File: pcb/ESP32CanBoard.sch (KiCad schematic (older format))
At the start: 46 parts, among them K1 1Wire, P1 Voltages, P101 CanBus, P2 Power, P3 CONN_1, P4 CONN_1, P5 CONN_1, P6 CONN_1, U1 ESP32Dev, U102 TJA1050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

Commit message: Just before switching away from ESP32 ADC
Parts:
- removed C5, C6: 100nF, Capacitors_SMD:C_0805_HandSoldering, symbol C
- removed JP1: ADC_CAL, Pin_Headers:Pin_Header_Straight_2x01, symbol JUMPER
- removed P1: Voltages, Connect:bornier6, symbol CONN_6
- removed R12, R13: 1M, Resistors_SMD:R_0805_HandSoldering, symbol R
- removed R5, R6: 220K, Resistors_SMD:R_0805_HandSoldering, symbol R
- added P102: CONN_4, Connect:bornier4, symbol CONN_4
- added U101: ADS1115, Divers:ADS1115, symbol ADS1115
- R1, R2, R3, R4: value 220K -> 22K
- R10, R7, R8, R9: value 1M -> 100K
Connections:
- net labels removed: ADC0, ADC1, ADC2, ADC3, ADC4, ADC5, DAC_Calibration, VIN0, VIN1, VIN2, VIN3, VIN4, VIN5
- wire segments 128 -> 106
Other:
- note added: "15*2.2/12.2=2.7049v\nRemove for shunt measurements"
- note added: "A0-A3 have ESD capable of sinking max 10mA. \nWith 100K that allows the inputs to see 1KV before any damage is done.\nHence no external diodes required.\nInternal resistance of the ADC at 4v FSD is 6M single ended, 15M double ended. At 0.256v Single ended the interal resistance is 100M\nBoth single and double ended will measure + - voltages."
- note added: "Measuring Voltage can be single ended, but measuring a shunt may\nhave to be differential since there will be voltage drop over the negative\nsupply line between the shunt and the pcd, unless the pcb has its -ve at the shunt."

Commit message: New board, moved bme280 to CanPressure board
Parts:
- removed C1, C2, C3, C4: 100nF, Capacitors_SMD:C_0805_HandSoldering, symbol C
- removed P101: CanBus, Connect:bornier2, symbol CONN_2
- removed P2: Power, Connect:bornier2, symbol CONN_2
- removed R1, R2, R3, R4: 22K, Resistors_SMD:R_0805_HandSoldering, symbol R
- removed R10, R7, R8, R9: 100K, Resistors_SMD:R_0805_HandSoldering, symbol R
- removed U101: ADS1115, Divers:ADS1115, symbol ADS1115
- removed U2: BMP280, Divers:BMP280, symbol BMP280
- added C101: 100nF, Capacitors_SMD:C_0805, symbol C
- added D103, D104: SMBJ30CA-TR TSV, Diodes_SMD:DO-214AB, symbol DIODE
- added D105: 1N5819, Diodes_SMD:D_1206, symbol DIODE
- added IC101: SP3481CN, Housings_SOIC:SOIC-8_3.9x4.9mm_Pitch1.27mm, symbol SP3481CN
- added P101: CAN, Connect:bornier4, symbol CONN_4
- added P103: Display, Pin_Headers:Pin_Header_Straight_1x05, symbol CONN_5
- added P104: Dsiplay, Pin_Headers:Pin_Header_Straight_1x08, symbol CONN_8
- added R101: 4K7, Resistors_SMD:R_0805, symbol R
- added TH101, TH102: Thermistor, Resistors_SMD:R_1812, symbol THERMISTOR
- C105: footprint Capacitors_SMD:C_0805_HandSoldering -> Capacitors_SMD:C_0805
- C205, C206: footprint Capacitors_SMD:C_1210_HandSoldering -> Capacitors_SMD:C_1210
- D101, D102, D203: footprint Diodes_SMD:DO-214AB_Handsoldering -> Diodes_SMD:DO-214AB
- D204: footprint Diodes_SMD:DO-214AB_Handsoldering -> Diodes_SMD:D_1206
- P102: value CONN_4 -> RS485
- R11, R14, R15, R16, R17: footprint Resistors_SMD:R_0805_HandSoldering -> Resistors_SMD:R_0805
- TH1, TH2: footprint Resistors_SMD:R_1210 -> Resistors_SMD:R_1812
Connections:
- net labels added: 5.8V, BL, BTN, CAN-H, CAN-L, CS, DC, MOSI, RS485-A, RS485-B, RS485-EN, RS485-RX, RS485-TX, RST, SCK
- wire segments 106 -> 113
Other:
- note removed: "15*2.2/12.2=2.7049v\nRemove for shunt measurements"
- note removed: "A0-A3 have ESD capable of sinking max 10mA. \nWith 100K that allows the inputs to see 1KV before any damage is done.\nHence no external diodes required.\nInternal resistance of the ADC at 4v FSD is 6M single ended, 15M double ended. At 0.256v Single ended the interal resistance is 100M\nBoth single and double ended will measure + - voltages."
- note removed: "Measuring Voltage can be single ended, but measuring a shunt may\nhave to be differential since there will be voltage drop over the negative\nsupply line between the shunt and the pcd, unless the pcb has its -ve at the shunt."

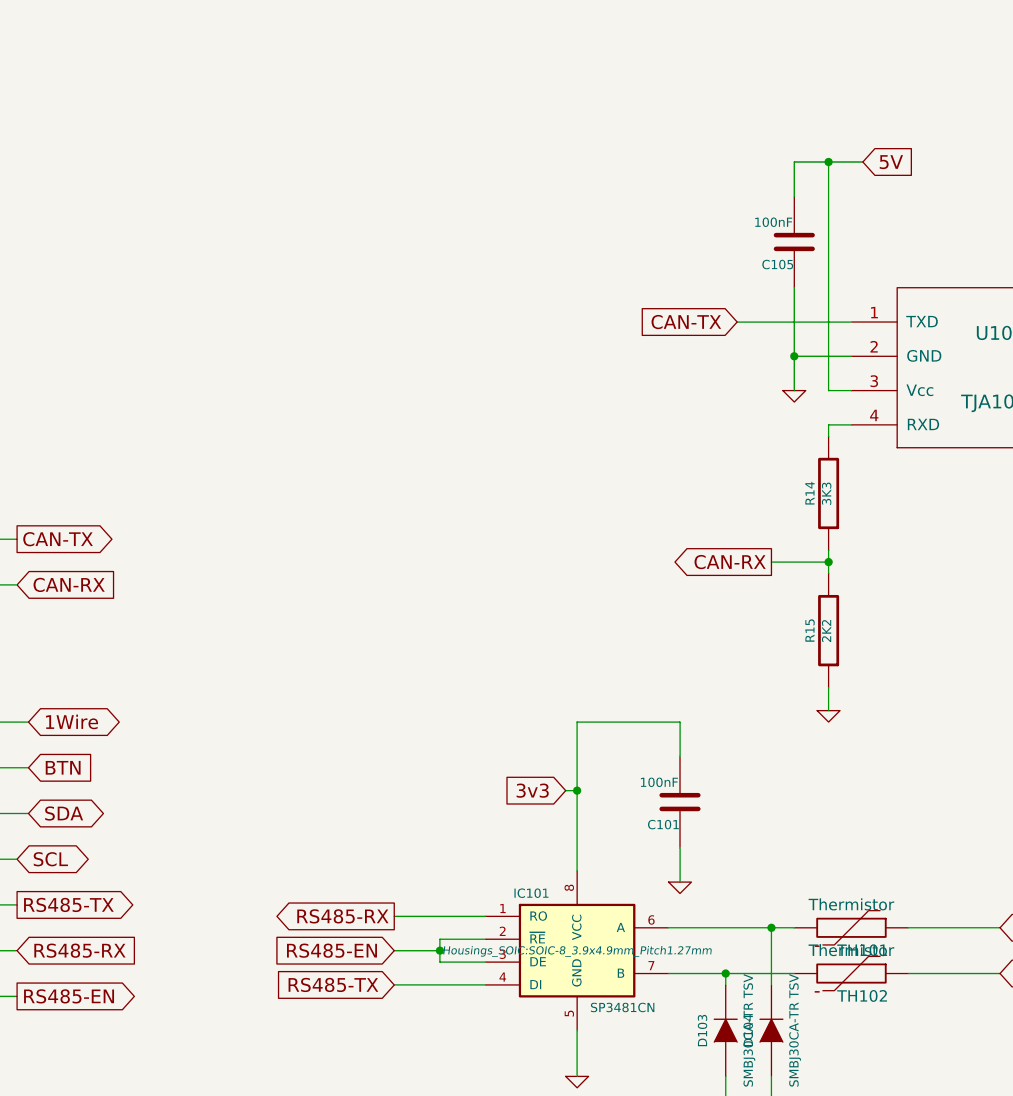
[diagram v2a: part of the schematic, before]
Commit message: New board operational using Modbus BatterySensors and CanPressure board
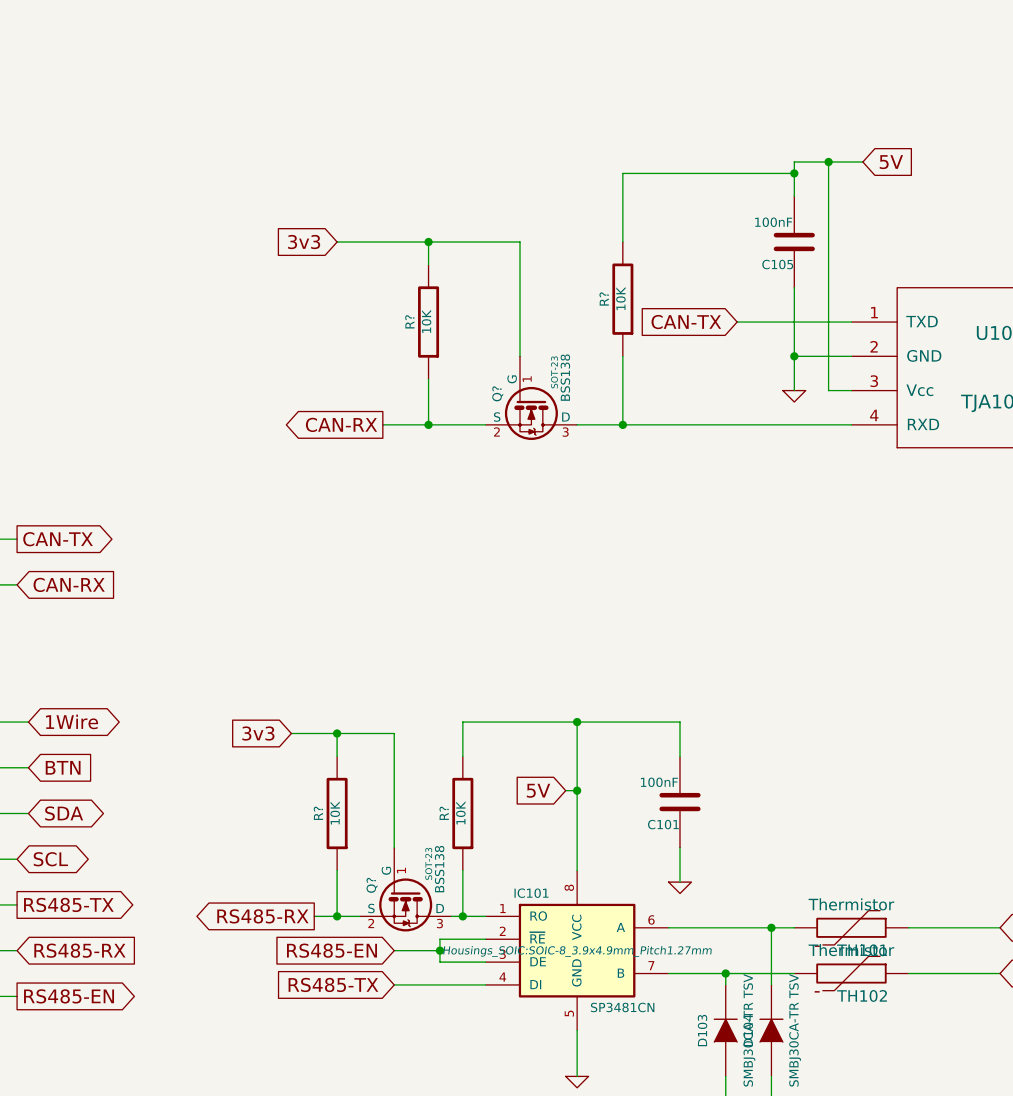
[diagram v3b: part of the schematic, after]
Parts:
- removed R14: 3K3, Resistors_SMD:R_0805, symbol R
- removed R15: 2K2, Resistors_SMD:R_0805, symbol R
- added Q? (x2): BSS138, SOT-23, symbol BSS138
- added R? (x4): 10K, Resistors_SMD:R_0805, symbol R
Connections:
- net 3v3: now also Q?.1 (G), Q?.1 (G), R?.2, R?.2; no longer C101.2, IC101.8 (VCC)
- net 5V: now also C101.2, IC101.8 (VCC), R?.2, R?.2
- net CAN-RX: now also Q?.2 (S), R?.1
- net RS485-RX: now also Q?.2 (S), R?.1; no longer IC101.1 (RO)
- net at U102.4 (RXD): now also Q?.3 (D), R?.1
- new net: IC101.1 (RO), Q?.3 (D), R?.1
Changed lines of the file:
@@
 Connection ~ 10650 3800
 Wire Wire Line
-	10650 3100 10650 2950
+	10650 2950 10650 3100
 Wire Wire Line
 	10650 2950 10950 2950
@@
 Text GLabel 10400 3650 0    60   Input ~ 0
 CAN-TX
-$Comp
-L R R14
-U 1 1 618128F6
-P 10800 4400
-F 0 "R14" V 10880 4400 40  0000 C CNN
-F 1 "3K3" V 10807 4401 40  0000 C CNN
-F 2 "Resistors_SMD:R_0805" V 10730 4400 30  0001 C CNN
-F 3 "" H 10800 4400 30  0000 C CNN
-	1    10800 4400
-	-1   0    0    1
-$EndComp
-$Comp
-L R R15
-U 1 1 618129BF
-P 10800 5000
-F 0 "R15" V 10880 5000 40  0000 C CNN
-F 1 "2K2" V 10807 5001 40  0000 C CNN
-F 2 "Resistors_SMD:R_0805" V 10730 5000 30  0001 C CNN
-F 3 "" H 10800 5000 30  0000 C CNN
-	1    10800 5000
-	-1   0    0    1
-$EndComp
-Wire Wire Line
-	10900 4100 10800 4100
-Wire Wire Line
-	10800 4100 10800 4150
-Wire Wire Line
-	10800 4650 10800 4750
-$Comp
-L GND #PWR010
-U 1 1 61812E4A
-P 10800 5350
-F 0 "#PWR010" H 10800 5350 30  0001 C CNN
-F 1 "GND" H 10800 5280 30  0001 C CNN
-F 2 "" H 10800 5350 60  0001 C CNN
-F 3 "" H 10800 5350 60  0001 C CNN
-	1    10800 5350
-	1    0    0    -1
-$EndComp
-Wire Wire Line
-	10800 5350 10800 5250
-Text GLabel 10550 4700 0    60   Output ~ 0
+Text GLabel 8850 4100 0    60   Output ~ 0
 CAN-RX
-Wire Wire Line
-	10800 4700 10550 4700
-Connection ~ 10800 4700
 $Comp
 L CONN_1 P3
@@
 	9700 6750 9700 6950
 Text GLabel 9650 5700 0    60   Input ~ 0
-3v3
+5V
 Wire Wire Line
 	9650 5700 9700 5700
@@
 Wire Wire Line
 	8900 6550 9300 6550
-Text GLabel 8900 6250 0    60   Output ~ 0
+Text GLabel 8550 6250 0    60   Output ~ 0
 RS485-RX
 Text GLabel 8900 6400 0    60   Input ~ 0
@@
 	8900 6400 9100 6400
 Connection ~ 9100 6400
-Wire Wire Line
-	8900 6250 9300 6250
 Text GLabel 7250 6600 2    60   Output ~ 0
 RS485-EN
@@
 $EndComp
 Wire Wire Line
-	9700 5400 10150 5400
+	9200 5400 10150 5400
 Wire Wire Line
 	10150 5400 10150 5550
@@
 Text GLabel 3400 6800 0    60   Output ~ 0
 RST
+$Comp
+L BSS138 Q?
+U 1 1 62D10656
+P 9500 4000
+F 0 "Q?" H 9500 3851 40  0000 R CNN
+F 1 "BSS138" H 9500 4150 40  0000 R CNN
+F 2 "SOT-23" H 9370 4102 29  0000 C CNN
+F 3 "" H 9500 4000 60  0000 C CNN
+	1    9500 4000
+	0    1    1    0
+$EndComp
+$Comp
+L R R?
+U 1 1 62D10E07
+P 9900 3550
+F 0 "R?" V 9980 3550 40  0000 C CNN
+F 1 "10K" V 9907 3551 40  0000 C CNN
+F 2 "Resistors_SMD:R_0805" V 9830 3550 30  0001 C CNN
+F 3 "" H 9900 3550 30  0000 C CNN
+	1    9900 3550
+	-1   0    0    1
+$EndComp
+$Comp
+L R R?
+U 1 1 62D10FA8
+P 9050 3650
+F 0 "R?" V 9130 3650 40  0000 C CNN
+F 1 "10K" V 9057 3651 40  0000 C CNN
+F 2 "Resistors_SMD:R_0805" V 8980 3650 30  0001 C CNN
+F 3 "" H 9050 3650 30  0000 C CNN
+	1    9050 3650
+	-1   0    0    1
+$EndComp
+Wire Wire Line
+	8850 4100 9300 4100
+Wire Wire Line
+	9050 3900 9050 4100
+Connection ~ 9050 4100
+Wire Wire Line
+	9450 3300 9450 3800
+Wire Wire Line
+	8650 3300 9450 3300
+Wire Wire Line
+	9050 3300 9050 3400
+Wire Wire Line
+	9700 4100 10900 4100
+Wire Wire Line
+	9900 3800 9900 4100
+Connection ~ 9900 4100
+Wire Wire Line
+	9900 3300 9900 3000
+Wire Wire Line
+	9900 3000 10650 3000
+Connection ~ 10650 3000
+$Comp
+L BSS138 Q?
+U 1 1 62D120FB
+P 8950 6150
+F 0 "Q?" H 8950 6001 40  0000 R CNN
+F 1 "BSS138" H 8950 6300 40  0000 R CNN
+F 2 "SOT-23" H 8820 6252 29  0000 C CNN
+F 3 "" H 8950 6150 60  0000 C CNN
+	1    8950 6150
+	0    1    1    0
+$EndComp
+Wire Wire Line
+	9150 6250 9300 6250
+Wire Wire Line
+	8550 6250 8750 6250
+Text GLabel 8650 3300 0    60   Input ~ 0
+3v3
+Connection ~ 9050 3300
+$Comp
+L R R?
+U 1 1 62D12BA0
+P 8650 5800
+F 0 "R?" V 8730 5800 40  0000 C CNN
+F 1 "10K" V 8657 5801 40  0000 C CNN
+F 2 "Resistors_SMD:R_0805" V 8580 5800 30  0001 C CNN
+F 3 "" H 8650 5800 30  0000 C CNN
+	1    8650 5800
+	-1   0    0    1
+$EndComp
+Text GLabel 8450 5450 0    60   Input ~ 0
+3v3
+$Comp
+L R R?
+U 1 1 62D12EBB
+P 9200 5800
+F 0 "R?" V 9280 5800 40  0000 C CNN
+F 1 "10K" V 9207 5801 40  0000 C CNN
+F 2 "Resistors_SMD:R_0805" V 9130 5800 30  0001 C CNN
+F 3 "" H 9200 5800 30  0000 C CNN
+	1    9200 5800
+	-1   0    0    1
+$EndComp
+Wire Wire Line
+	9200 5400 9200 5550
+Connection ~ 9700 5400
+Wire Wire Line
+	9200 6050 9200 6250
+Connection ~ 9200 6250
+Wire Wire Line
+	8650 6050 8650 6250
+Connection ~ 8650 6250
+Wire Wire Line
+	8650 5550 8650 5450
+Wire Wire Line
+	8450 5450 8900 5450
+Wire Wire Line
+	8900 5450 8900 5950
+Connection ~ 8650 5450
 $EndSCHEMATC

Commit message: Fixed display
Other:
- note added: "Pin RXD is driven so this level shifter is strictly \nnot required and could be replaced by a R divider.\n\n3v into TXD is high enough for 5V logic.\n"
- note added: "RO is high impedence when RE/DE \nare high, so a level shifter is required."
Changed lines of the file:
@@
 	8900 5450 8900 5950
 Connection ~ 8650 5450
+Text Notes 8050 5300 0    60   ~ 0
+RO is high impedence when RE/DE \nare high, so a level shifter is required.
+Text Notes 8700 4550 0    60   ~ 0
+Pin RXD is driven so this level shifter is strictly \nnot required and could be replaced by a R divider.\n\n3v into TXD is high enough for 5V logic.\n
 $EndSCHEMATC

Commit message: Adapted to new modbus shunt modules and tested over 10m wire
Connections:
- net RST: now also U1.10 (ADC2_CH7/GPIO27); no longer U1.12 (GPIO12/must_be_low_on_onboot/hspi_miso)
- net BSY: now reaches U1.5 (ADC1_7/GPIO35_In_only)
- net BSY: now also P104.1 (P1)
- net BL: no longer names the net of U1.13 (GPIO13/MTCK_dont_use/hspi_mosi)
- net BL: no longer P104.1 (P1)
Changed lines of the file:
@@
 Wire Wire Line
 	2350 6650 2350 6700
-Text GLabel 1900 7250 2    60   Input ~ 0
-BL
-Text GLabel 3400 7000 0    60   Output ~ 0
-BL
+Text GLabel 1900 7250 2    60   Output ~ 0
+BSY
+Text GLabel 3400 5400 0    60   Input ~ 0
+BSY
 Text GLabel 3400 6200 0    60   Output ~ 0
 DC
-Text GLabel 3400 6800 0    60   Output ~ 0
+Text GLabel 3400 6400 0    60   Output ~ 0
 RST
 $Comp
